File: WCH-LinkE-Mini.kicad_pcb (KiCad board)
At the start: 2 copper layers, 38.1 x 15.2 mm, 38 parts, among them J2 Conn_02x05_Odd_Even, J3 USB_C_Receptacle_USB2.0_16P, Q1 AO3401A, Q2 AO3401A, Q3 AO3401A, SW1 SW_Push, SW2 SW_Push, U2 CH32V305FBP6, U5 XC6206P332MR-G, Y2 12M

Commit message: fix silk
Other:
- board text added: "WCH-LinkE-Mini"
- board text removed: "WCH-LinkE"
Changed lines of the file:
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@@
 		)
 	)
-	(gr_text "WCH-LinkE"
-		(at 132.588 125.73 -0)
+	(gr_text "WCH-LinkE-Mini"
+		(at 129.159 125.73 0)
 		(layer "B.SilkS")
 		(effects
@@
 				(thickness 0.15)
 			)
-			(justify mirror)
+			(justify right mirror)
 		)
 	)

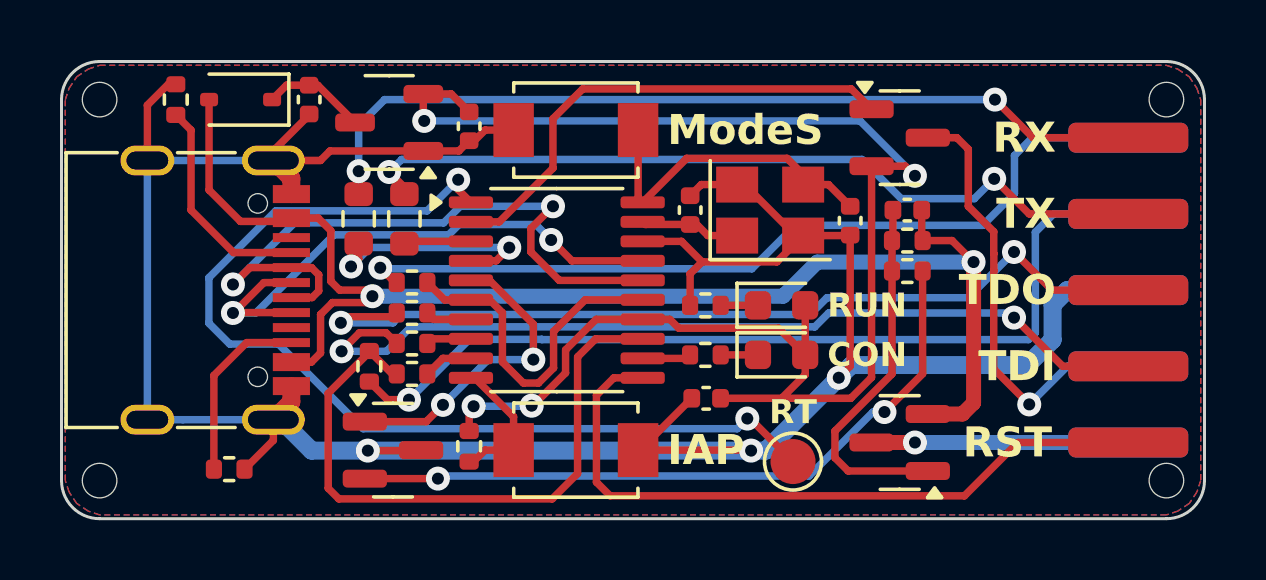
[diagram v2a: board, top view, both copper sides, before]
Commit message: change load switch structure
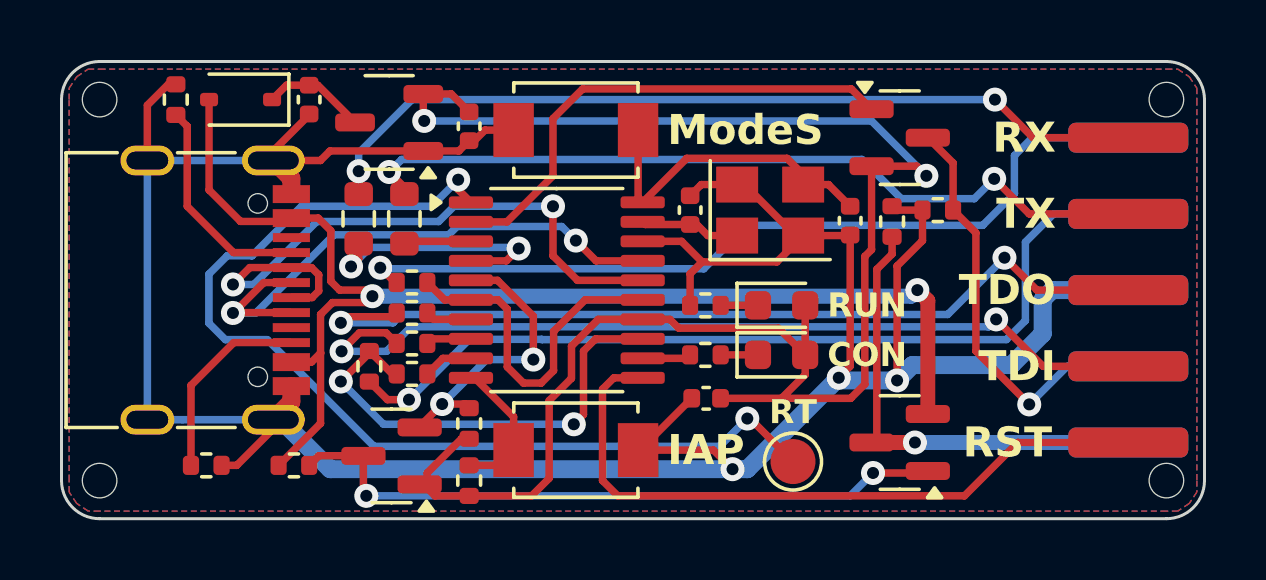
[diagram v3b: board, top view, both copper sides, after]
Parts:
- removed C6: 0.1u, Capacitor_SMD:C_0402_1005Metric
- added R15: 10k, Resistor_SMD:R_0402_1005Metric, F.Cu at (156.2, 116.7)
- added R16: 10k, Resistor_SMD:R_0402_1005Metric, F.Cu at (154.7, 117.1)
- Q3: value AO3401A -> BSS138
- R14: value 22k -> 10k
- moved R14 21.4 mm to (134.7, 125.2)
- moved R13 15.8 mm to (140.6, 123.8), turned to -90 degrees
- moved R10 1.14 mm to (140.6, 125.7), turned to 90 degrees
- moved R12 0.77 mm to (131.8, 125.2)
- moved Q3 0.20 mm to (138.0, 124.9), turned to 180 degrees
- renumbered J3 to J1, U5 to U1, Y2 to Y1
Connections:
- Q2 pad 1: Net-(Q2-G) -> /PB12_5V
- Q3 pad 1: /PB12 -> +3V3
- Q3 pad 2: Net-(Q3-S) -> /PB12
- Q3 pad 3: GND -> /PB12_5V
- R13 pad 1: +5V -> /PB12
- R13 pad 2: Net-(Q2-G) -> +3V3
- R14 pad 1: Net-(Q2-G) -> +5V
- R14 pad 2: Net-(Q3-S) -> /PB12_5V
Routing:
- net Net-(Q3-S): track 23.5 -> 0.00 mm, vias 2 -> 0
- net /PB12_5V: track 0.00 -> 22.6 mm, vias 0 -> 2
- net Net-(Q2-G): track 12.3 -> 0.00 mm
- net /5V_OUT: track 8.56 -> 15.7 mm
- net +3V3: track 51.3 -> 58.1 mm, vias 4 -> 2
- net GND: track 94.0 -> 99.9 mm
- net /D_SWDIO: track 21.5 -> 15.7 mm, vias 0 -> 2
- net +5V: track 45.3 -> 42.2 mm
- net /USB_N: track 22.4 -> 21.5 mm
- net /PB12: track 10.3 -> 9.52 mm
- net Net-(U2-PB11): track 7.78 -> 8.41 mm
- net /3V3_OUT: track 14.7 -> 14.1 mm
- net Net-(U2-~{RST}): track 33.8 -> 34.3 mm
- net /RX: track 28.8 -> 28.3 mm
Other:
- board text added: "WCH-LinkE-Mini v1.1.0"
- board text removed: "WCH-LinkE-Mini"

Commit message: add resettable fuse
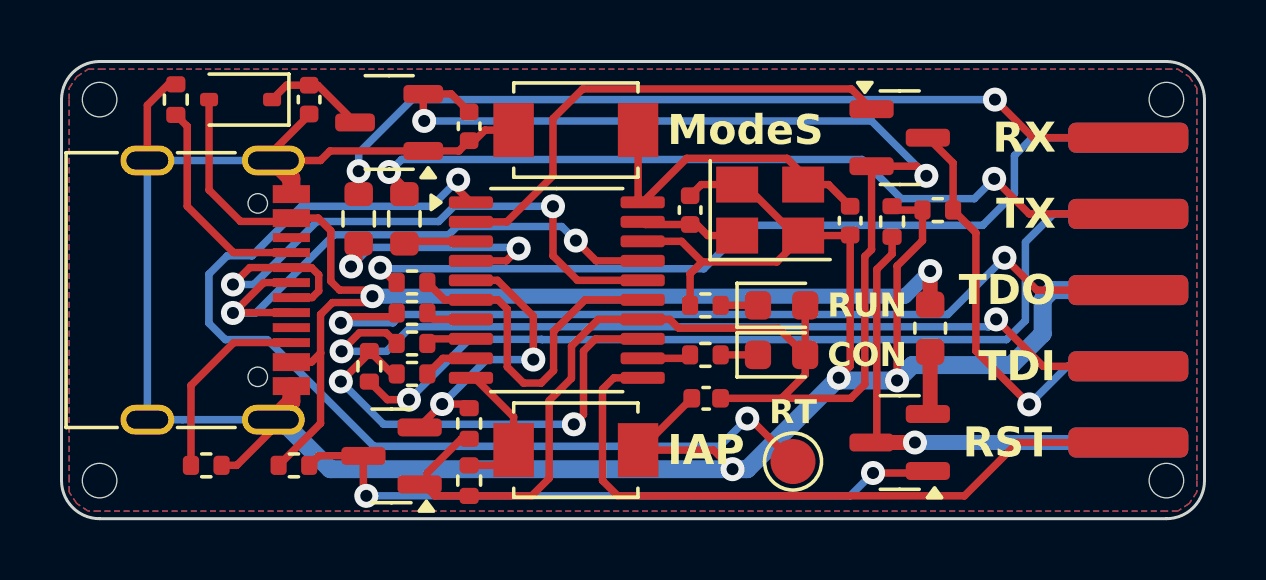
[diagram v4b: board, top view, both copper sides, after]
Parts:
- added F1: 350mA, Fuse:Fuse_0603_1608Metric, F.Cu at (156.0, 120.7)
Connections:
- Q2 pad 2: +5V -> Net-(Q2-S)
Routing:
- net +5V: track 42.2 -> 39.7 mm
- net Net-(Q2-S): track 0.00 -> 2.11 mm
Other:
- board text added: "WCH-LinkE-Mini v1.2.0"
- board text removed: "WCH-LinkE-Mini v1.1.0"

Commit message: v1.3.0 (#3)
* v1.3.0

* Create review.yml

* remove yml
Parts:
- removed F1: 350mA, Fuse:Fuse_0603_1608Metric
- D3: value 1N5819WS -> B5819WS
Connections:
- C2 pad 1: Net-(D3-K) -> +5V
- D3 pad 1: Net-(D3-K) -> +5V
- D3 pad 2: +5V -> Net-(D3-A)
- J1 pad A4: +5V -> Net-(D3-A)
- J1 pad A9: +5V -> Net-(D3-A)
- J1 pad B4: +5V -> Net-(D3-A)
- J1 pad B9: +5V -> Net-(D3-A)
- Q2 pad 2: Net-(Q2-S) -> +5V
- U1 pad 3: Net-(D3-K) -> +5V
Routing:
- net +5V: track 39.7 -> 56.4 mm, vias 2 -> 3
- net Net-(D3-A): track 0.00 -> 14.5 mm, vias 0 -> 2
- net Net-(U2-~{RST}): track 34.3 -> 38.5 mm
- net Net-(D3-K): track 3.48 -> 0.00 mm
- net Net-(U2-PB11): track 8.41 -> 11.8 mm
- net Net-(Q2-S): track 2.11 -> 0.00 mm
- net /PA5: track 16.6 -> 18.5 mm
- net /SWCLK/TCK: track 28.3 -> 30.1 mm
- net /TX: track 27.1 -> 25.6 mm
- net /TDI: track 29.6 -> 30.7 mm
- net /TDO: track 29.6 -> 30.4 mm
- net +3V3: track 58.1 -> 57.4 mm
- net /USB_P: track 19.6 -> 18.9 mm
- net GND: track 99.9 -> 99.4 mm
- net Net-(J1-CC2): track 6.60 -> 7.11 mm
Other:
- board text added: "WCH-LinkE-Mini v1.3.0"
- board text removed: "WCH-LinkE-Mini v1.2.0"

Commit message: v1.3.0
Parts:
- added R17: 10k, Resistor_SMD:R_0402_1005Metric, F.Cu at (133.2, 125.7)
- added R18: 10k, Resistor_SMD:R_0402_1005Metric, F.Cu at (155.3, 116.6)
- R15, R16: value 10k -> 330
- moved R16 21.9 mm to (134.7, 126.2), turned to 0 degrees
- moved R15 1.26 mm to (155.3, 117.6)
- moved R12 1.02 mm to (130.8, 125.2), turned to 0 degrees
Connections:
- Q1 pad 1: /PA5 -> Net-(Q1-G)
- Q2 pad 1: /PB12_5V -> Net-(Q2-G)
- R15 pad 1: /3V3_OUT -> Net-(Q1-G)
- R15 pad 2: GND -> /PA5
- R16 pad 1: /5V_OUT -> Net-(Q2-G)
- R16 pad 2: GND -> /PB12_5V
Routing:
- net Net-(Q2-G): track 0.00 -> 26.1 mm, vias 0 -> 2
- net /PB12_5V: track 22.6 -> 3.21 mm, vias 2 -> 0
- net Net-(Q1-G): track 0.00 -> 11.3 mm, vias 0 -> 2
- net GND: track 99.4 -> 91.9 mm, vias 3 -> 2
- net /5V_OUT: track 15.7 -> 8.56 mm
- net +3V3: track 57.4 -> 55.6 mm
- net +5V: track 56.4 -> 55.0 mm
- net Net-(U2-PB11): track 11.8 -> 10.6 mm
- net /PA5: track 18.5 -> 19.5 mm, vias 0 -> 2
- net Net-(U2-~{RST}): track 38.5 -> 37.6 mm

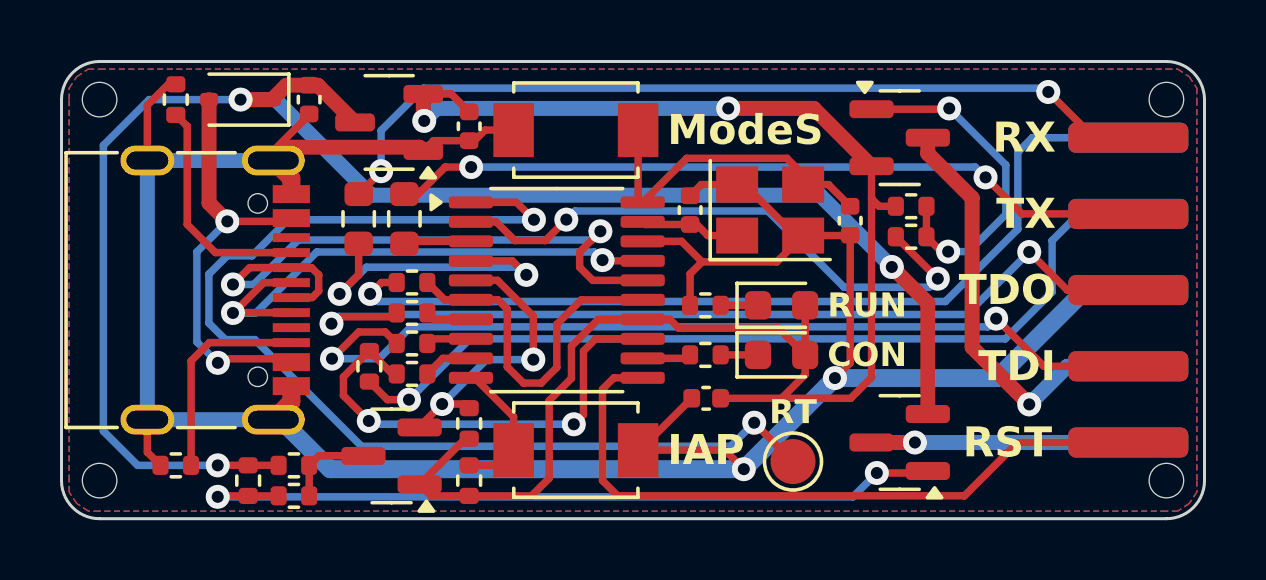
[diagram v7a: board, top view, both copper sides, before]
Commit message: update symbols and footprints
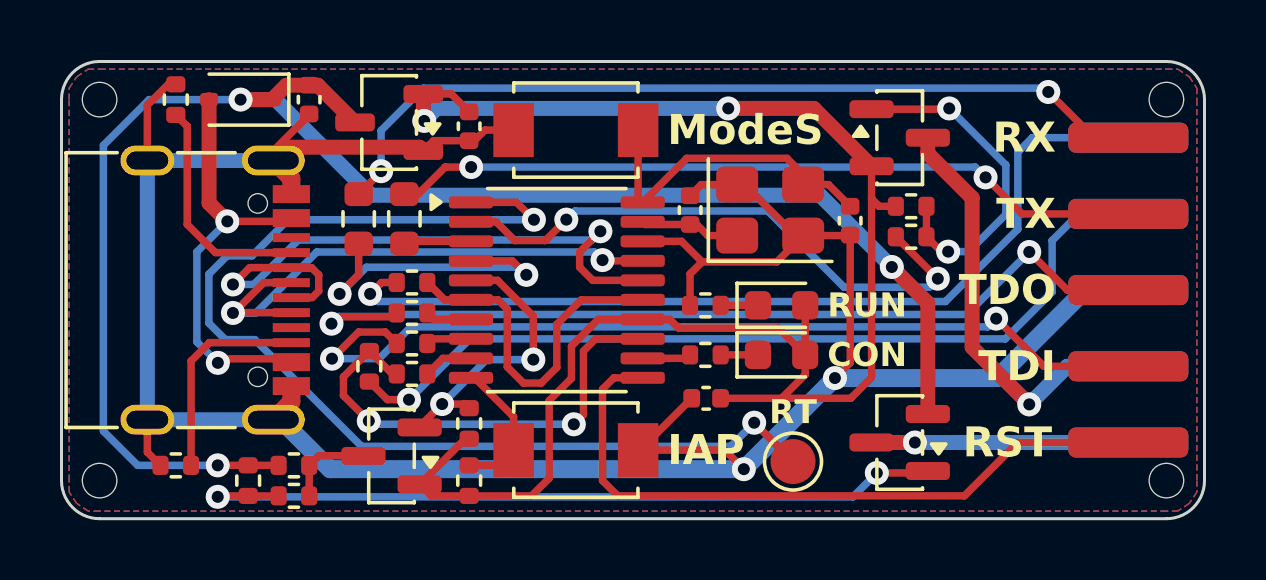
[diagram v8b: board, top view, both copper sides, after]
